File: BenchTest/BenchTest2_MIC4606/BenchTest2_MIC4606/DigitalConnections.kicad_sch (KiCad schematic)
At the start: 35 parts, among them J8 Conn_01x10, U13 SRV05-4, U14 SRV05-4

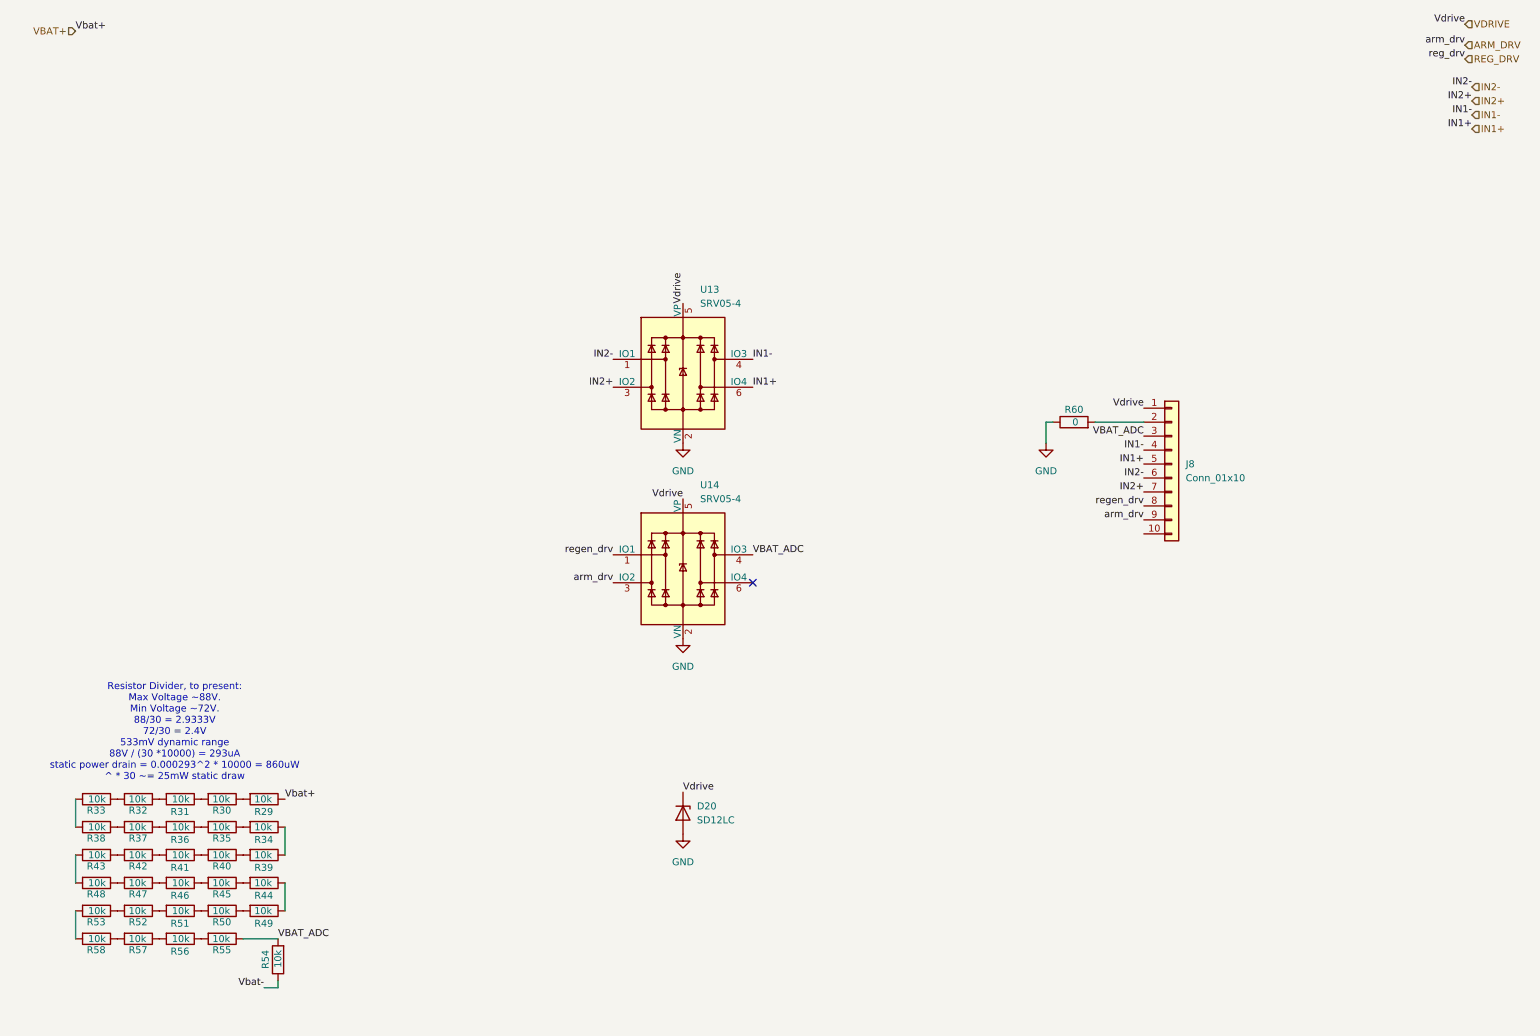
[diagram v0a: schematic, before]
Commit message: Added motor voltage measurement for regen
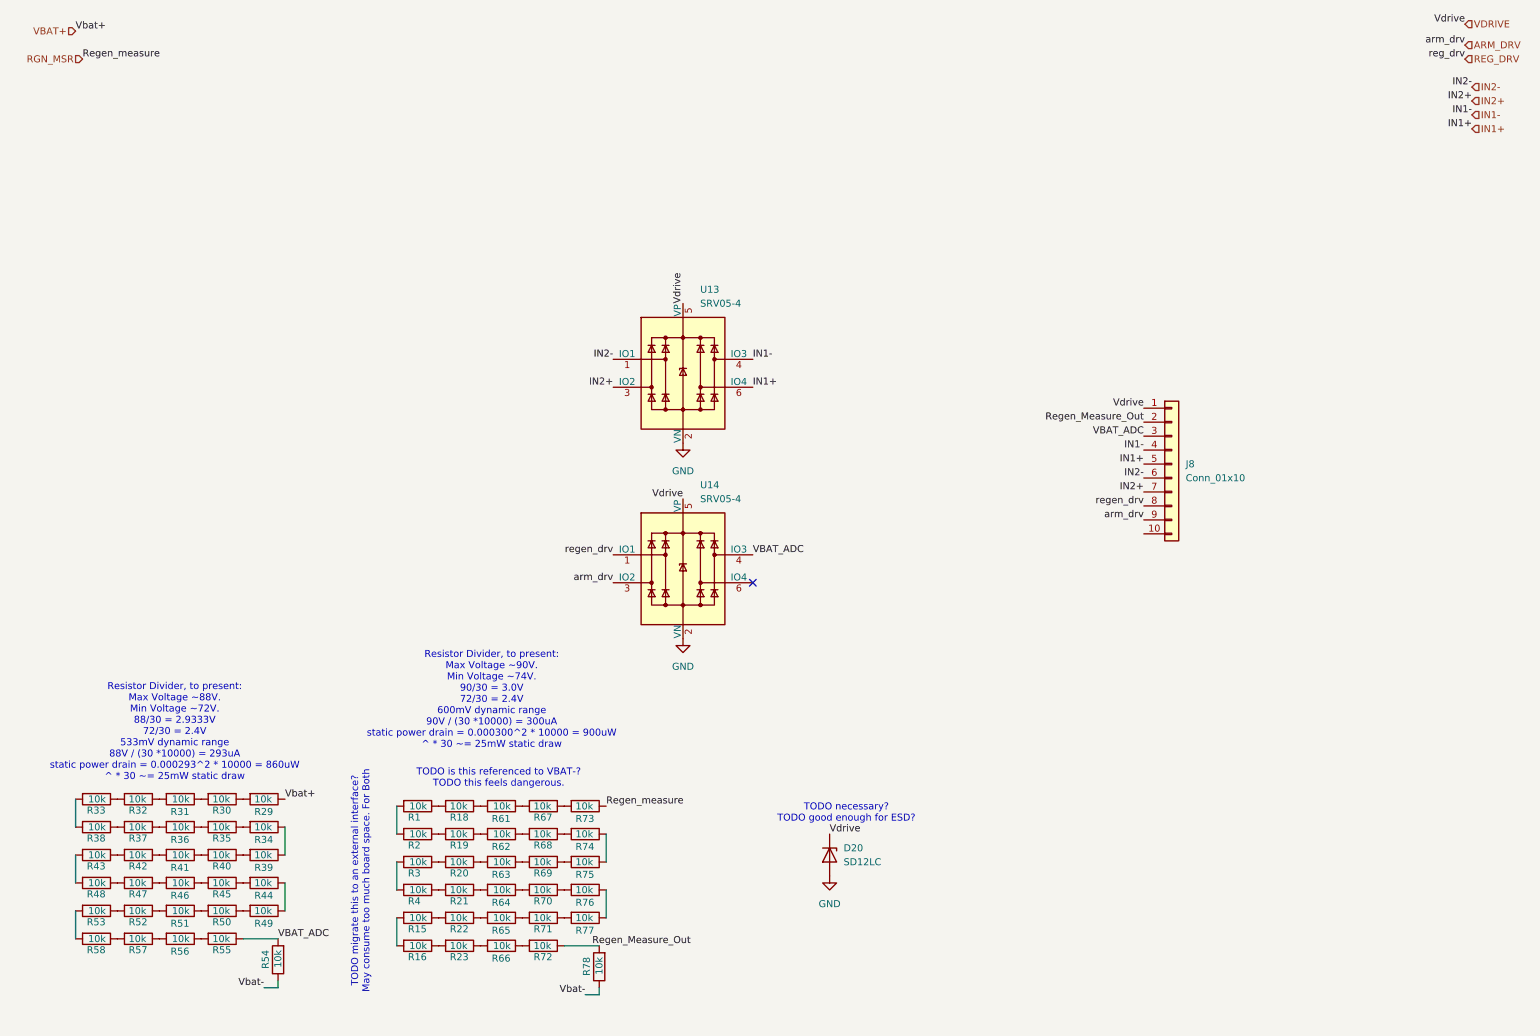
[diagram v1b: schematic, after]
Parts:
- removed R60: 0, symbol Device:R
- added R1, R15, R16, R18, R19, R2, R20, R21, R22, R23, R3, R4, R61, R62, R63, R64, R65, R66, R67, R68, R69, R70, R71, R72, R73, R74, R75, R76, R77, R78: 10k, Resistor_SMD:R_0603_1608Metric_Pad0.98x0.95mm_HandSolder, symbol Device:R
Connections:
- net Vbat-: now also R78.1
- net Regen_Measure_Out: now reaches J8.2 (Pin_2)
- net Regen_Measure_Out: now also R72.1, R78.2
- new net: R16.1, R23.2
- new net: R15.2, R16.2
- new net: R23.1, R66.2
- new net: R67.1, R73.2
- new net: R1.1, R18.2
- new net: R1.2, R2.2
- new net: R22.1, R65.2
- new net: R15.1, R22.2
- new net: R66.1, R72.2
- new net: R64.1, R70.2
- new net: R21.1, R64.2
- new net: R68.1, R74.2
- new net: R62.1, R68.2
- new net: R61.1, R67.2
- new net: R18.1, R61.2
- new net: R19.1, R62.2
- new net: R71.1, R77.2
- new net: R65.1, R71.2
- new net: R63.1, R69.2
- new net: R20.1, R63.2
- new net: R20.2, R3.1
- new net: R74.1, R75.1
- new net: R69.1, R75.2
- new net: R19.2, R2.1
- new net: R21.2, R4.1
- new net: R3.2, R4.2
- new net: R76.1, R77.1
- new net: R70.1, R76.2
- new net RGN_MSR: R73.1
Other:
- note added: "Resistor Divider, to present: Max Voltage ~90V. Min Voltage ~74V. 90/30 = 3.0V 72/30 = 2.4V 600mV dynamic range 90V / (30 *10000) = 300uA static power drain = 0.000300^2 * 10000 = 900uW ^ * 30 ~= 25mW static draw"
- note added: "TODO is this referenced to VBAT-? TODO this feels dangerous."
- note added: "TODO migrate this to an external interface? May consume too much board space. For Both"
- note added: "TODO necessary? TODO good enough for ESD?"
- moved on the sheet: D20

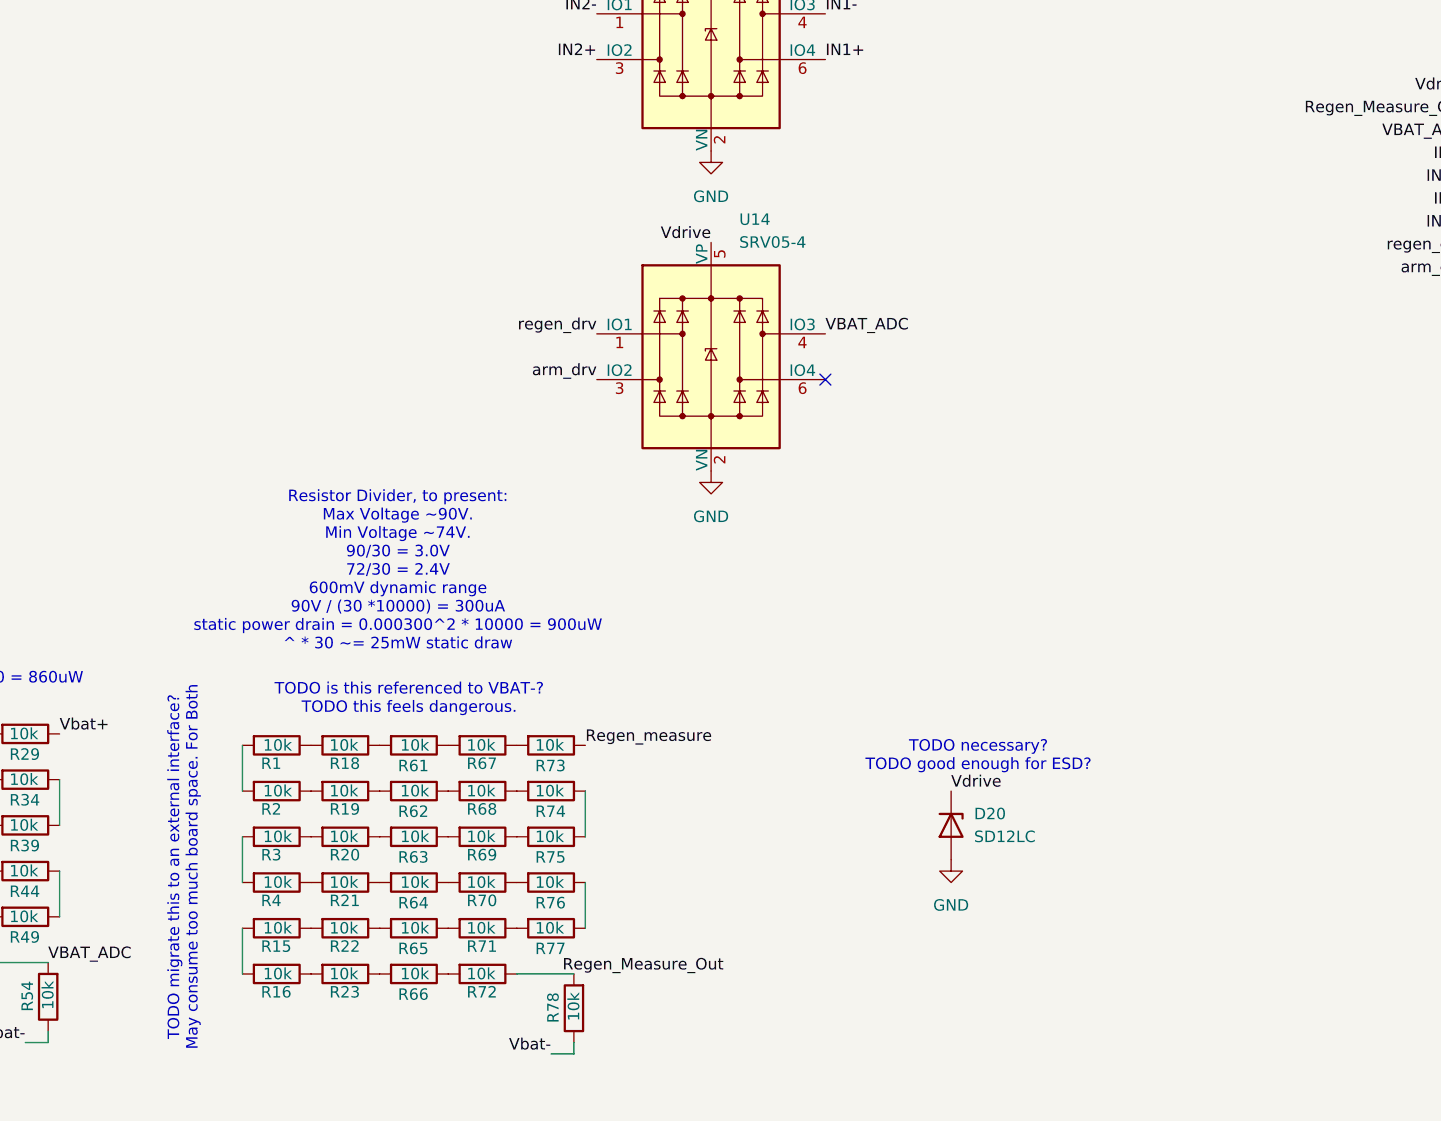
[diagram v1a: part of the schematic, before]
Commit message: Added VMOT Measurements
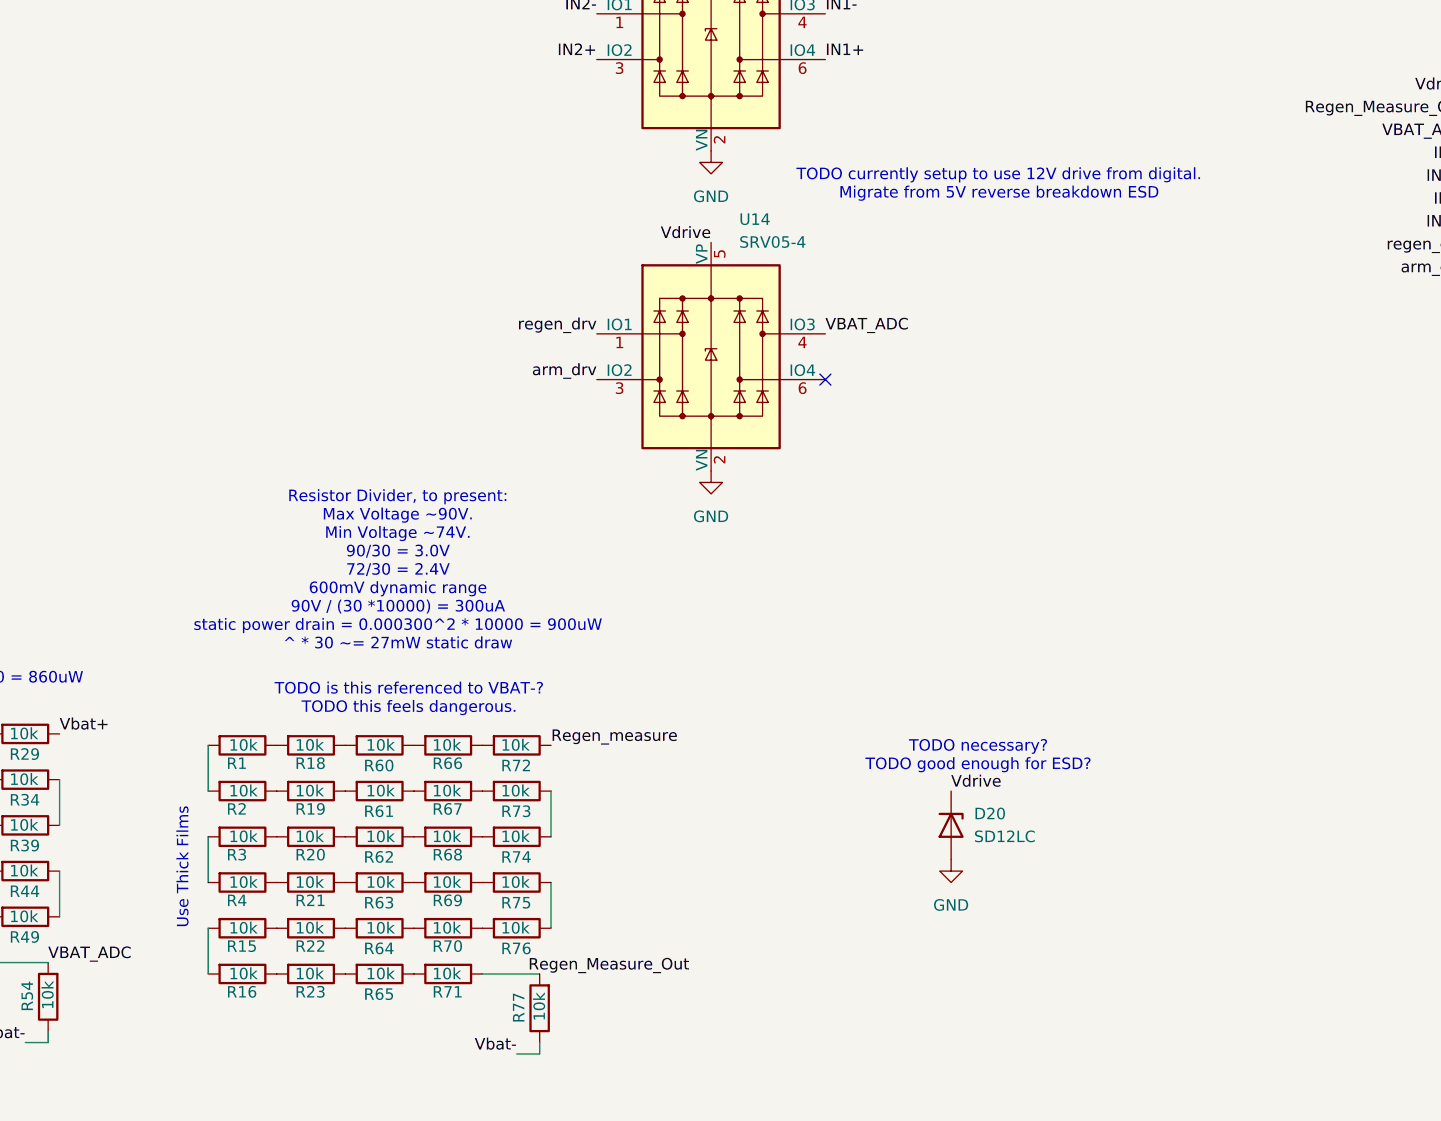
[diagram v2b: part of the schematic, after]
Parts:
- removed R78: 10k, Resistor_SMD:R_0603_1608Metric_Pad0.98x0.95mm_HandSolder, symbol Device:R
- added R60: 10k, Resistor_SMD:R_0201_0603Metric_Pad0.64x0.40mm_HandSolder, symbol Device:R
- R1, R15, R16, R18, R19, R2, R20, R21, R22, R23, R29, R3, R30, R31, R32, R33, R35, R36, R37, R38, R39, R4, R40, R41, R42, R43, R44, R45, R46, R47, R48, R49, R50, R51, R52, R53, R54, R55, R56, R57, R58, R61, R62, R63, R64, R65, R66, R67, R68, R69, R70, R71, R72, R74, R75, R76, R77: footprint Resistor_SMD:R_0603_1608Metric_Pad0.98x0.95mm_HandSolder -> Resistor_SMD:R_0201_0603Metric_Pad0.64x0.40mm_HandSolder
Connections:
- net RGN_MSR: now also R72.1; no longer R73.1
- net Regen_Measure_Out: now also R71.1, R77.2; no longer R72.1
- net Vbat-: now also R77.1
- net at R66.2: now also R60.1; no longer R23.1
- net at R65.2: now also R23.1; no longer R22.1
- net at R21.1: now also R63.2; no longer R64.2
- net at R18.1: now also R60.2; no longer R61.2
- net at R62.2: now also R20.1; no longer R19.1
- net at R75.1: now also R76.1; no longer R74.1
- new net: R22.1, R64.2
- new net: R73.1, R74.1
- new net: R19.1, R61.2
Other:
- note added: "Resistor Divider, to present: Max Voltage ~90V. Min Voltage ~74V. 90/30 = 3.0V 72/30 = 2.4V 600mV dynamic range 90V / (30 *10000) = 300uA static power drain = 0.000300^2 * 10000 = 900uW ^ * 30 ~= 27mW static draw"
- note added: "TODO currently setup to use 12V drive from digital. Migrate from 5V reverse breakdown ESD"
- note added: "Use Thick Films"
- note removed: "Resistor Divider, to present: Max Voltage ~90V. Min Voltage ~74V. 90/30 = 3.0V 72/30 = 2.4V 600mV dynamic range 90V / (30 *10000) = 300uA static power drain = 0.000300^2 * 10000 = 900uW ^ * 30 ~= 25mW static draw"
- note removed: "TODO migrate this to an external interface? May consume too much board space. For Both"
